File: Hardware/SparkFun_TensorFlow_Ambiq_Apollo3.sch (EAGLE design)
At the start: 71 parts, among them J5 CORTEX_DEBUG, J6 CAMERA-OV7670, U2 LIS2DH12, U3 1.8V, U5 ARTEMIS_MODULESMD, Y2 32.768kHz

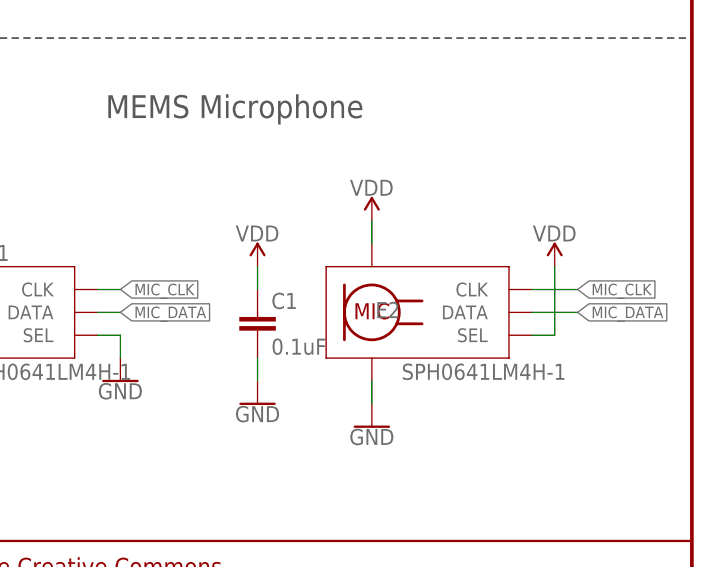
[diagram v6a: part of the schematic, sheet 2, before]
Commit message: Invert JTAG connector
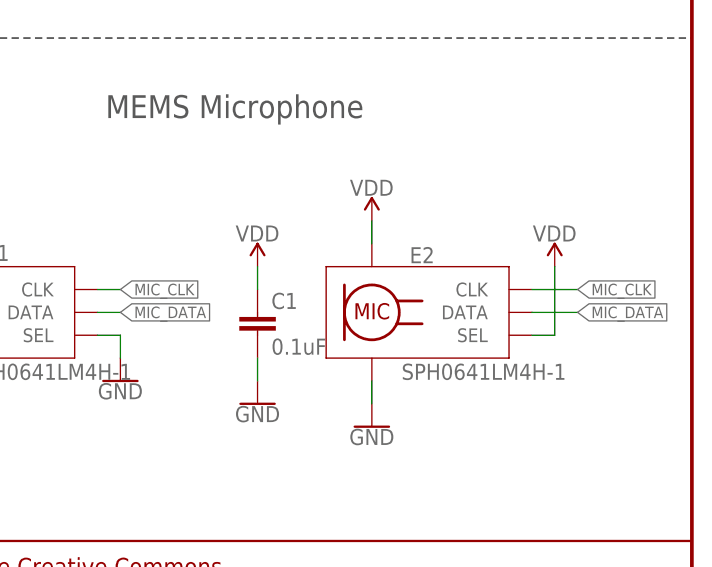
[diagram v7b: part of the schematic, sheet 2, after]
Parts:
- J5: device SparkFun-Connectors:CORTEX_DEBUG_MINIMUM_PTH_NS -> SparkFun-Connectors:CORTEX_DEBUG_MINIMUM_PTH
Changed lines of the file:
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@@
 <grid distance="0.1" unitdist="inch" unit="inch" style="lines" multiple="1" display="no" altdistance="0.01" altunitdist="inch" altunit="inch"/>
 <layers>
-<layer number="1" name="Top" color="4" fill="1" visible="no" active="no"/>
-<layer number="2" name="Route2" color="22" fill="3" visible="no" active="no"/>
-<layer number="3" name="Route3" color="4" fill="3" visible="no" active="no"/>
-<layer number="4" name="Route4" color="1" fill="4" visible="no" active="no"/>
-<layer number="5" name="Route5" color="4" fill="4" visible="no" active="no"/>
-<layer number="6" name="Route6" color="1" fill="8" visible="no" active="no"/>
-<layer number="7" name="Route7" color="4" fill="8" visible="no" active="no"/>
-<layer number="8" name="Route8" color="1" fill="2" visible="no" active="no"/>
-<layer number="9" name="Route9" color="4" fill="2" visible="no" active="no"/>
-<layer number="10" name="Route10" color="1" fill="7" visible="no" active="no"/>
-<layer number="11" name="Route11" color="4" fill="7" visible="no" active="no"/>
-<layer number="12" name="Route12" color="1" fill="5" visible="no" active="no"/>
-<layer number="13" name="Route13" color="4" fill="5" visible="no" active="no"/>
-<layer number="14" name="Route14" color="1" fill="6" visible="no" active="no"/>
-<layer number="15" name="Route15" color="14" fill="6" visible="no" active="no"/>
-<layer number="16" name="Bottom" color="1" fill="1" visible="no" active="no"/>
-<layer number="17" name="Pads" color="2" fill="1" visible="no" active="no"/>
-<layer number="18" name="Vias" color="2" fill="1" visible="no" active="no"/>
-<layer number="19" name="Unrouted" color="6" fill="1" visible="no" active="no"/>
-<layer number="20" name="Dimension" color="24" fill="1" visible="no" active="no"/>
-<layer number="21" name="tPlace" color="16" fill="1" visible="no" active="no"/>
-<layer number="22" name="bPlace" color="14" fill="1" visible="no" active="no"/>
-<layer number="23" name="tOrigins" color="15" fill="1" visible="no" active="no"/>
-<layer number="24" name="bOrigins" color="15" fill="1" visible="no" active="no"/>
-<layer number="25" name="tNames" color="7" fill="1" visible="no" active="no"/>
-<layer number="26" name="bNames" color="7" fill="1" visible="no" active="no"/>
-<layer number="27" name="tValues" color="7" fill="1" visible="no" active="no"/>
-<layer number="28" name="bValues" color="7" fill="1" visible="no" active="no"/>
+<layer number="1" name="Top" color="4" fill="1" visible="yes" active="no"/>
+<layer number="2" name="Route2" color="22" fill="3" visible="yes" active="no"/>
+<layer number="3" name="Route3" color="4" fill="3" visible="yes" active="no"/>
+<layer number="4" name="Route4" color="1" fill="4" visible="yes" active="no"/>
+<layer number="5" name="Route5" color="4" fill="4" visible="yes" active="no"/>
+<layer number="6" name="Route6" color="1" fill="8" visible="yes" active="no"/>
+<layer number="7" name="Route7" color="4" fill="8" visible="yes" active="no"/>
+<layer number="8" name="Route8" color="1" fill="2" visible="yes" active="no"/>
+<layer number="9" name="Route9" color="4" fill="2" visible="yes" active="no"/>
+<layer number="10" name="Route10" color="1" fill="7" visible="yes" active="no"/>
+<layer number="11" name="Route11" color="4" fill="7" visible="yes" active="no"/>
+<layer number="12" name="Route12" color="1" fill="5" visible="yes" active="no"/>
+<layer number="13" name="Route13" color="4" fill="5" visible="yes" active="no"/>
+<layer number="14" name="Route14" color="1" fill="6" visible="yes" active="no"/>
+<layer number="15" name="Route15" color="14" fill="6" visible="yes" active="no"/>
+<layer number="16" name="Bottom" color="1" fill="1" visible="yes" active="no"/>
+<layer number="17" name="Pads" color="2" fill="1" visible="yes" active="no"/>
+<layer number="18" name="Vias" color="2" fill="1" visible="yes" active="no"/>
+<layer number="19" name="Unrouted" color="6" fill="1" visible="yes" active="no"/>
+<layer number="20" name="Dimension" color="24" fill="1" visible="yes" active="no"/>
+<layer number="21" name="tPlace" color="16" fill="1" visible="yes" active="no"/>
+<layer number="22" name="bPlace" color="14" fill="1" visible="yes" active="no"/>
+<layer number="23" name="tOrigins" color="15" fill="1" visible="yes" active="no"/>
+<layer number="24" name="bOrigins" color="15" fill="1" visible="yes" active="no"/>
+<layer number="25" name="tNames" color="7" fill="1" visible="yes" active="no"/>
+<layer number="26" name="bNames" color="7" fill="1" visible="yes" active="no"/>
+<layer number="27" name="tValues" color="7" fill="1" visible="yes" active="no"/>
+<layer number="28" name="bValues" color="7" fill="1" visible="yes" active="no"/>
 <layer number="29" name="tStop" color="7" fill="3" visible="no" active="no"/>
 <layer number="30" name="bStop" color="7" fill="6" visible="no" active="no"/>
@@
 <layer number="35" name="tGlue" color="7" fill="4" visible="no" active="no"/>
 <layer number="36" name="bGlue" color="7" fill="5" visible="no" active="no"/>
-<layer number="37" name="tTest" color="7" fill="1" visible="no" active="no"/>
-<layer number="38" name="bTest" color="7" fill="1" visible="no" active="no"/>
+<layer number="37" name="tTest" color="7" fill="1" visible="yes" active="no"/>
+<layer number="38" name="bTest" color="7" fill="1" visible="yes" active="no"/>
 <layer number="39" name="tKeepout" color="4" fill="11" visible="no" active="no"/>
 <layer number="40" name="bKeepout" color="1" fill="11" visible="no" active="no"/>
@@
 <layer number="44" name="Drills" color="7" fill="1" visible="no" active="no"/>
 <layer number="45" name="Holes" color="7" fill="1" visible="no" active="no"/>
-<layer number="46" name="Milling" color="3" fill="1" visible="no" active="no"/>
-<layer number="47" name="Measures" color="7" fill="1" visible="no" active="no"/>
-<layer number="48" name="Document" color="7" fill="1" visible="no" active="no"/>
-<layer number="49" name="Reference" color="7" fill="1" visible="no" active="no"/>
-<layer number="50" name="dxf" color="7" fill="1" visible="no" active="no"/>
-<layer number="51" name="tDocu" color="6" fill="1" visible="no" active="no"/>
-<layer number="52" name="bDocu" color="7" fill="1" visible="no" active="no"/>
-<layer number="53" name="tGND_GNDA" color="7" fill="9" visible="no" active="no"/>
-<layer number="54" name="bGND_GNDA" color="1" fill="9" visible="no" active="no"/>
-<layer number="56" name="wert" color="7" fill="1" visible="no" active="no"/>
-<layer number="57" name="tCAD" color="7" fill="1" visible="no" active="no"/>
-<layer number="59" name="tCarbon" color="7" fill="1" visible="no" active="no"/>
-<layer number="60" name="bCarbon" color="7" fill="1" visible="no" active="no"/>
+<layer number="46" name="Milling" color="3" fill="1" visible="yes" active="no"/>
+<layer number="47" name="Measures" color="7" fill="1" visible="yes" active="no"/>
+<layer number="48" name="Document" color="7" fill="1" visible="yes" active="no"/>
+<layer number="49" name="Reference" color="7" fill="1" visible="yes" active="no"/>
+<layer number="50" name="dxf" color="7" fill="1" visible="yes" active="no"/>
+<layer number="51" name="tDocu" color="6" fill="1" visible="yes" active="no"/>
+<layer number="52" name="bDocu" color="7" fill="1" visible="yes" active="no"/>
+<layer number="53" name="tGND_GNDA" color="7" fill="9" visible="yes" active="no"/>
+<layer number="54" name="bGND_GNDA" color="1" fill="9" visible="yes" active="no"/>
+<layer number="56" name="wert" color="7" fill="1" visible="yes" active="no"/>
+<layer number="57" name="tCAD" color="7" fill="1" visible="yes" active="no"/>
+<layer number="59" name="tCarbon" color="7" fill="1" visible="yes" active="no"/>
+<layer number="60" name="bCarbon" color="7" fill="1" visible="yes" active="no"/>
 <layer number="88" name="SimResults" color="9" fill="1" visible="yes" active="yes"/>
 <layer number="89" name="SimProbes" color="9" fill="1" visible="yes" active="yes"/>
@@
 <part name="GND36" library="SparkFun-PowerSymbols" deviceset="GND" device=""/>
 <part name="GND37" library="SparkFun-PowerSymbols" deviceset="GND" device=""/>
-<part name="J5" library="SparkFun-Connectors" deviceset="CORTEX_DEBUG_MINIMUM" device="_PTH_NS" value="CORTEX_DEBUG"/>
+<part name="J5" library="SparkFun-Connectors" deviceset="CORTEX_DEBUG_MINIMUM" device="_PTH" value="CORTEX_DEBUG"/>
 <part name="C2" library="SparkFun-Capacitors" deviceset="0.1UF" device="-0402T-16V-10%" value="0.1uF"/>
 <part name="GND3" library="SparkFun-PowerSymbols" deviceset="GND" device=""/>
@@
 </instance>
 <instance part="E2" gate="E1" x="218.44" y="60.96" smashed="yes">
-<attribute name="NAME" x="215.138" y="61.214" size="1.778" layer="95" align="center"/>
+<attribute name="NAME" x="218.948" y="67.31" size="1.778" layer="95" align="center"/>
 <attribute name="VALUE" x="225.806" y="54.356" size="1.778" layer="96" align="center"/>
 </instance>

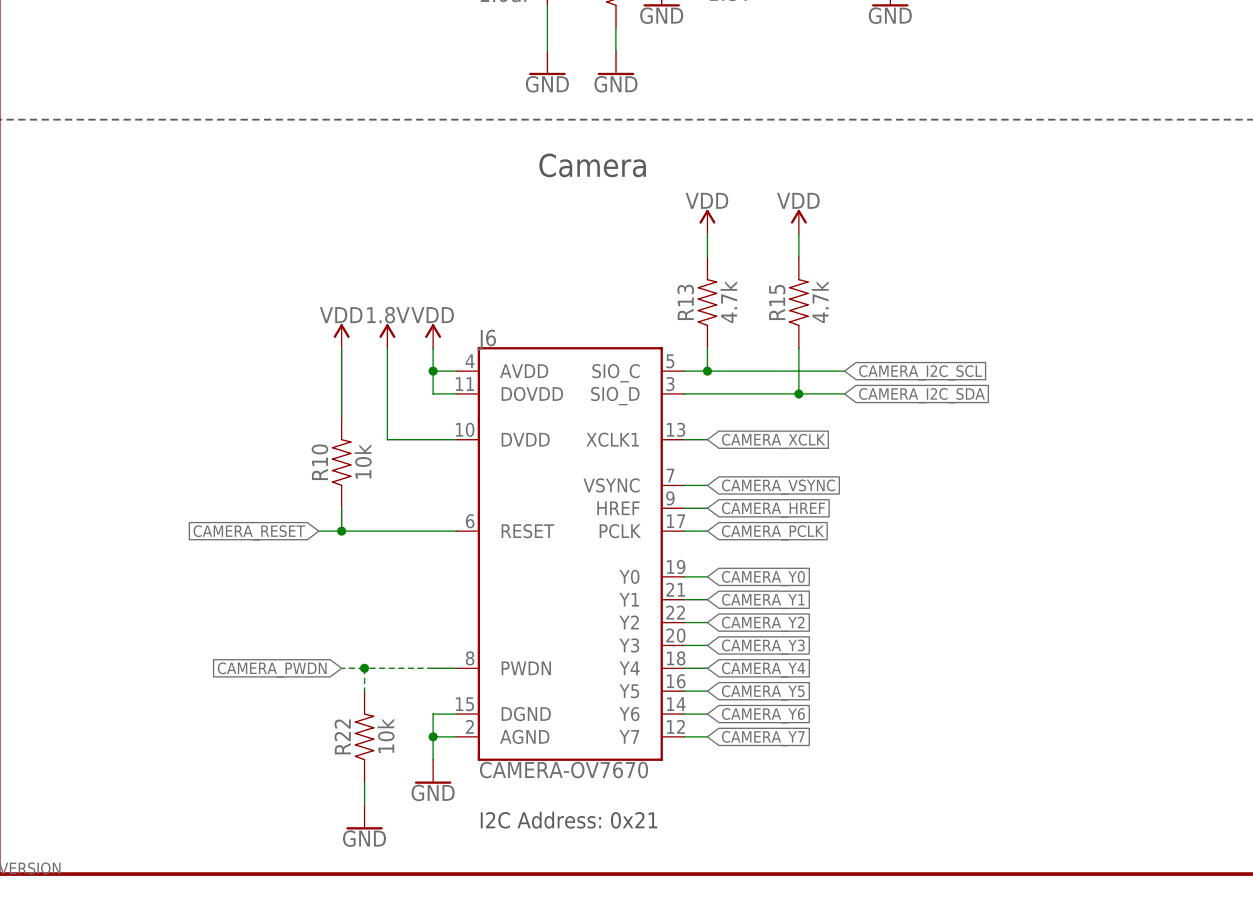
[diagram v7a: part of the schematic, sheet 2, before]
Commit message: Reroute camera interface to match himax spec
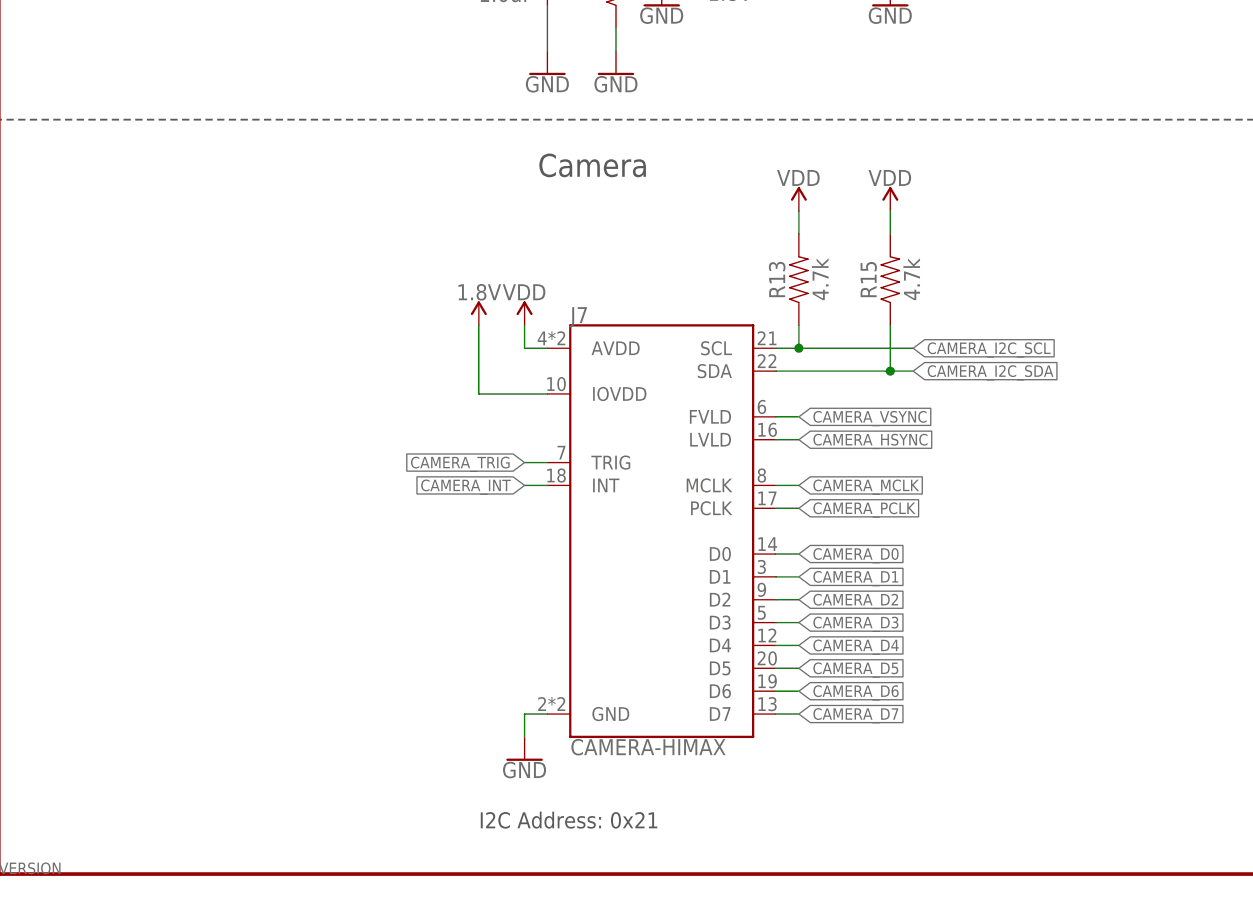
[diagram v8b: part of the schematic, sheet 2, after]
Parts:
- removed J6: CAMERA-OV7670, SparkFun-Connectors:CAMERA-OV7670
- removed R10, R22: 10k, SparkFun-Resistors:10KOHM-0402T-1/16W-1%
- removed R23, R24: 4.7k, SparkFun-Resistors:4.7KOHM-0603-1/10W-1%
- added J7: CAMERA-HIMAX, SparkFun-Connectors:CAMERA-HIMAX
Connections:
- removed net CAMERA_HREF: J6.HREF, U5.~AD13(I2SBCLK/RX1)
- removed net CAMERA_PWDN: J6.PWDN, R22.2, U5.(ADCD1N/RX1/PDMDATA)D15
- removed net CAMERA_RESET: J6.RESET, R10.1, U5.~AD11(PDMDATA)
- removed net CAMERA_XCLK: J6.XCLK1, U5.~AD32(SCCIO)
- removed net CAMERA_Y0: J6.Y0, U5.(PDMCLK/SWO)~D22
- removed net CAMERA_Y1: J6.Y1, U5.(RX1/SLINT)~D4
- removed net CAMERA_Y2: J6.Y2, U5.~AD35(TX1/I2SDAT/PDMCLK)
- removed net CAMERA_Y3: J6.Y3, U5.(TX1/32KHZ/SWO)~D24
- removed net CAMERA_Y4: J6.Y4, U5.(I2SWCLK/CMPOUT)~D23
- removed net CAMERA_Y5: J6.Y5, U5.(MOSI2/I2SWCLK)~D28
- removed net CAMERA_Y6: J6.Y6, U5.(SDA0/MISO0/I2SDAT)~D6
- removed net CAMERA_Y7: J6.Y7, U5.(SCCRST)~D26
- new net CAMERA_D0: J7.D0, U5.(ADCD1P/TX1/PDMCLK)D14
- new net CAMERA_D1: J7.D1, U5.AD34(CMPRF2/PDMDATA)
- new net CAMERA_D2: J7.D2, U5.(SDA2/MISO2/RX1)~D25
- new net CAMERA_D3: J7.D3, U5.(ADCD1N/RX1/PDMDATA)D15
- new net CAMERA_D4: J7.D4, U5.(SDA0/MISO0/I2SDAT)~D6
- new net CAMERA_D5: J7.D5, U5.(SCL0/SCK0)~D5
- new net CAMERA_D6: J7.D6, U5.~AD35(TX1/I2SDAT/PDMCLK)
- new net CAMERA_D7: J7.D7, U5.(MOSI2/I2SWCLK)~D28
- new net CAMERA_HSYNC: J7.LVLD, U5.(SCL2/SCK2)~D27
- new net CAMERA_INT: J7.INT, U5.(I2SWCLK/CMPOUT)~D23
- new net CAMERA_MCLK: J7.MCLK, U5.(SLSCK/SLSCL/CLKOUT)D0
- new net CAMERA_TRIG: J7.TRIG, U5.(SCCRST)~D26
- net 1.8V: now also J7.IOVDD; no longer J6.DVDD
- net CAMERA_DVDD_EN: now also U5.~AD32(SCCIO); no longer U5.(MOSI0/CLKOUT)~D7
- net CAMERA_I2C_SCL: now also J7.SCL, U5.(SCL1/SCK1/TX1/SCCLK)D8; no longer J6.SIO_C, U5.(SCL2/SCK2)~D27
- net CAMERA_I2C_SDA: now also J7.SDA, U5.(SDA1/MISO1/RX1/SCCIO)D9; no longer J6.SIO_D, U5.(SDA2/MISO2/RX1)~D25
- net CAMERA_PCLK: now also J7.PCLK, U5.(MOSI0/CLKOUT)~D7; no longer J6.PCLK, U5.(ADCD1P/TX1/PDMCLK)D14
- net CAMERA_VSYNC: now also J7.FVLD, U5.~AD13(I2SBCLK/RX1); no longer J6.VSYNC, U5.AD34(CMPRF2/PDMDATA)
- net GND: now also J7.GND; no longer J6.AGND, J6.DGND, R22.1
- net QWIIC_SCL: no longer R24.1
- net QWIIC_SDA: no longer R23.1
- net VDD: now also J7.AVDD; no longer J6.AVDD, J6.DOVDD, R10.2, R23.2, R24.2
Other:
- note added: "Coin Cell/Serial Power"
- note removed: "Coin Cell/FTDI Power"
- moved on the sheet: J4, R13, R15, TP3, TP4
